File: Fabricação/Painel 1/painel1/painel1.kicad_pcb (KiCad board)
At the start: 2 copper layers, 200 x 200 mm, 76 parts, among them J1 1-776087-1, J1 Conn_01x09_Male, J10 AUX_POWER, J2 Conn_01x02_Male, J2 Conn_01x09_Male, J3 Conn_01x04_Male, J4 Conn_01x04_Male, J4 DC_CONVERTER, J5 UART, J5 VBAT, J6 Conn_01x04_Male, J6 UNFUSED, J7 CS_POWER, J9 ISOL_POWER, U1 YAAJ_BluePill, U2 MP1584, U3 LM324, U4 LM324, U5 TJA1050-Module

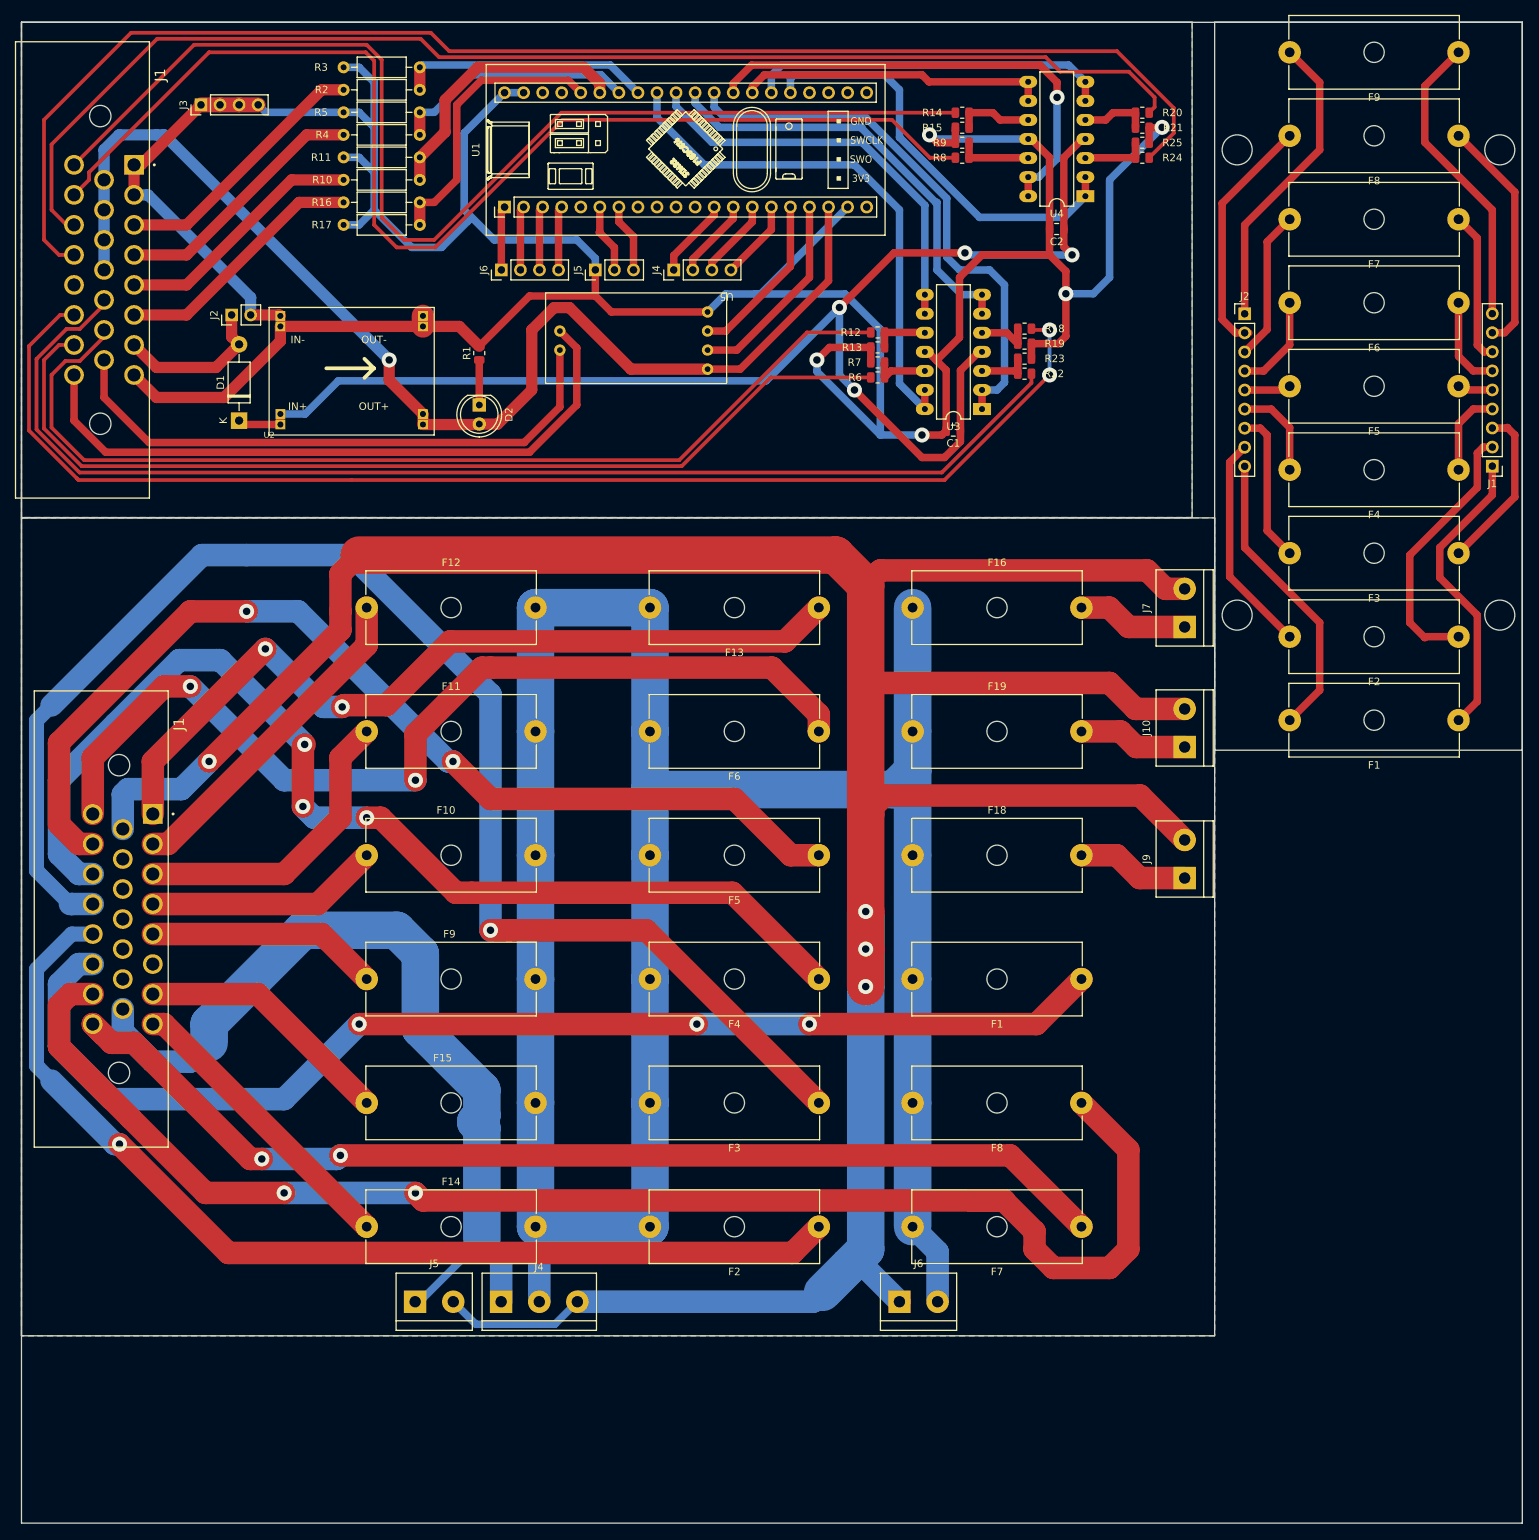
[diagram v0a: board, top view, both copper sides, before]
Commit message: FIX: panel border
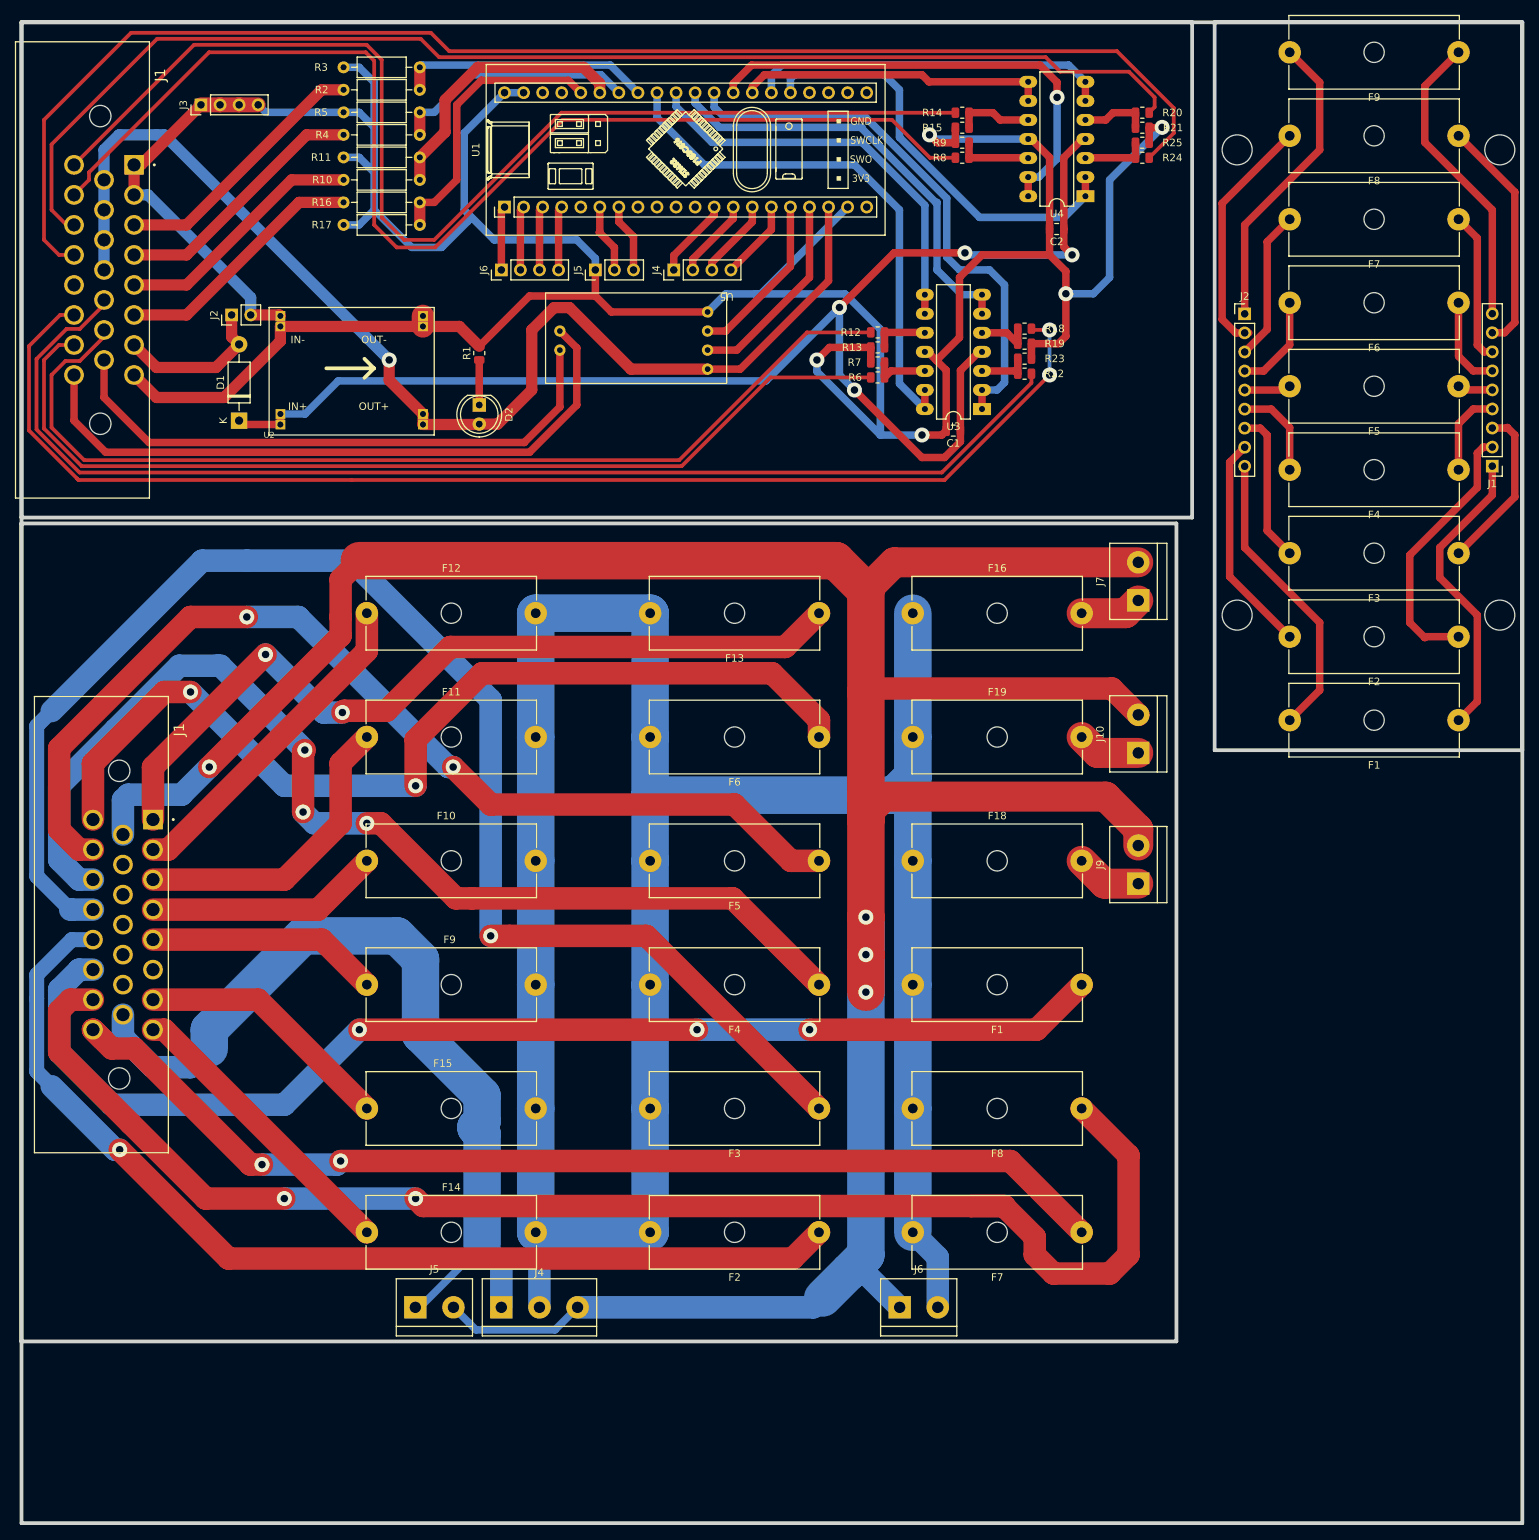
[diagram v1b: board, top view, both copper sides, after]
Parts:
- moved J7 7.12 mm to (178.8, 123.0)
- moved J10 6.23 mm to (178.8, 143.4)
- moved J9 6.22 mm to (178.8, 160.8)
- moved J5 0.75 mm to (82.5, 217.2)
- moved J1 0.75 mm to (47.5, 152.2)
- moved F1 0.75 mm to (171.3, 174.2)
- moved F10 0.75 mm to (76.0, 157.7)
- moved F11 0.75 mm to (76.0, 141.2)
- moved F14 0.75 mm to (76.0, 207.2)
- moved F15 0.75 mm to (76.0, 190.7)
- moved F18 0.75 mm to (148.8, 157.7)
- moved F19 0.75 mm to (148.8, 141.2)
- moved F2 0.75 mm to (136.3, 207.2)
- moved F3 0.75 mm to (136.3, 190.7)
- moved F4 0.75 mm to (136.3, 174.2)
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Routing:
- net (no net): track 6165.2 -> 6134.2 mm
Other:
- outline, holes or cut-outs redrawn
